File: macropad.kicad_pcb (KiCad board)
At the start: 2 copper layers, 40 x 140 mm, 64 parts, among them J1 SWD, J10 I2C, J11 Keyboard 1, J12 Keyboard 2, J13 Keyboard 2, J2 Keyboard 1, J3 Keyboard 2, J4 Keyboard 1, J5 UART, J6 RS485, J7 Extra, J8 USB_A, J9 CAN, SW1 SW_Push, SW10 Reset, SW2 SW_Push, SW3 SW_Push, SW4 SW_Push, SW5 SW_Push, SW6 SW_Push, U1 AP62250WU, U2 STM32F042K6Tx, U3 MAX490E, U4 MCP2551-I-SN

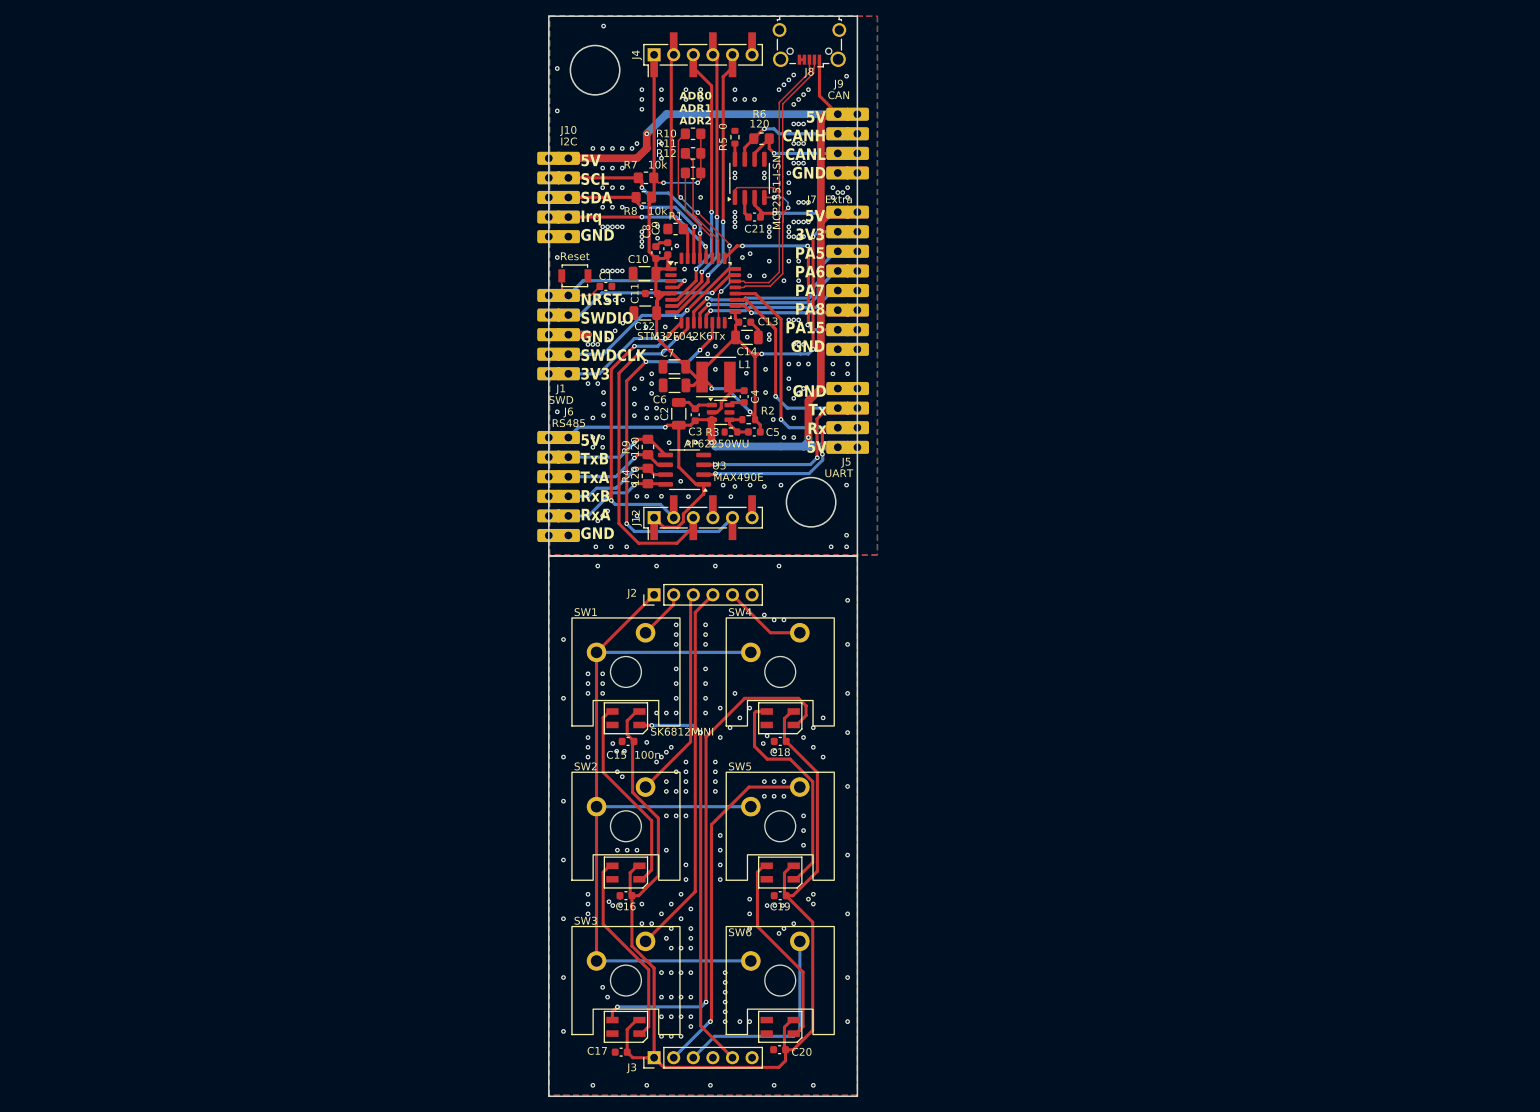
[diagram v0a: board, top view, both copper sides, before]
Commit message: - Created head board tilable up to 4x - Placed and routed lines ToDo: - Print - I2C reanbable
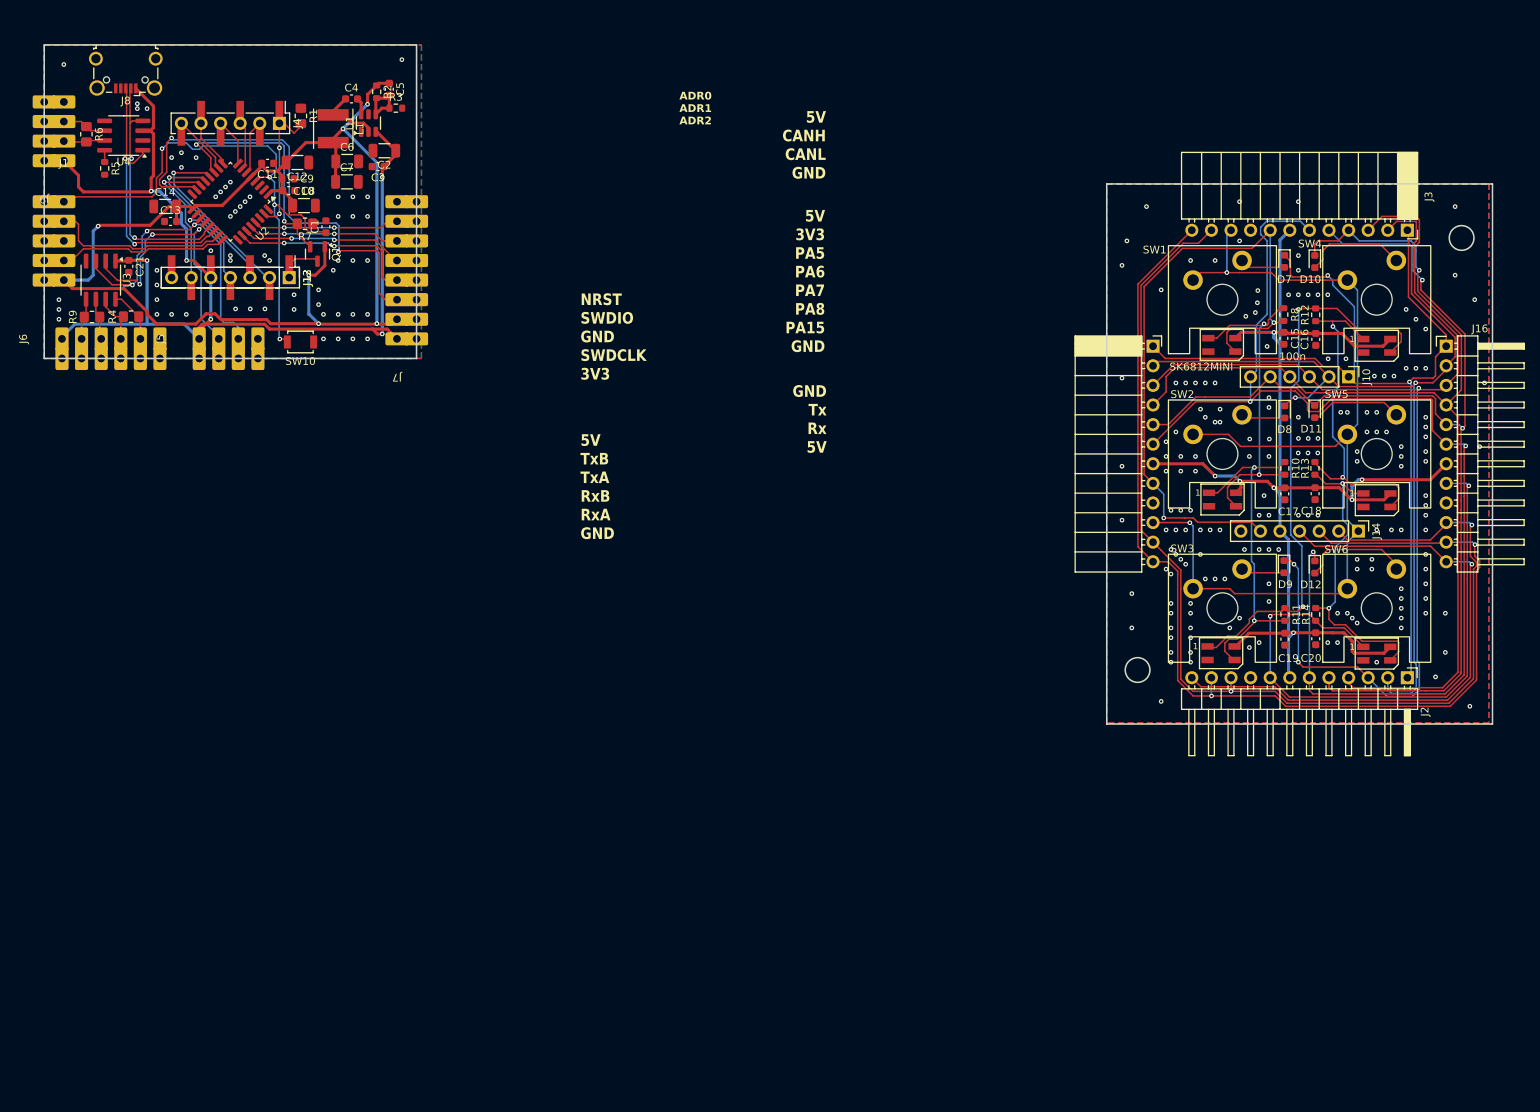
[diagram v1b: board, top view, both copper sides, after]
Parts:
- added D10: D, Diode_SMD:D_0603_1608Metric, F.Cu at (178.6, 73.7)
- added D11: D, Diode_SMD:D_0603_1608Metric, F.Cu at (178.6, 93.2)
- added D12: D, Diode_SMD:D_0603_1608Metric, F.Cu at (178.6, 113.3)
- added D7: D, Diode_SMD:D_0603_1608Metric, F.Cu at (174.6, 73.7)
- added D8: D, Diode_SMD:D_0603_1608Metric, F.Cu at (174.7, 93.2)
- added D9: D, Diode_SMD:D_0603_1608Metric, F.Cu at (174.6, 113.3)
- added J14: Keyboard 2, Connector_PinHeader_2.54mm:PinHeader_1x07_P2.54mm_Vertical, F.Cu at (184.2, 108.7)
- added J15: Conn_01x12_Socket, Connector_PinSocket_2.54mm:PinSocket_1x12_P2.54mm_Horizontal, F.Cu at (157.6, 84.7)
- added J16: Conn_01x12_Pin, Connector_PinHeader_2.54mm:PinHeader_1x12_P2.54mm_Horizontal, F.Cu at (195.6, 84.7)
- added Q1: PNP, Package_TO_SOT_SMD:SOT-23, F.Cu at (49.3, 72.7)
- added R13: R, Resistor_SMD:R_0603_1608Metric, F.Cu at (178.6, 100.5)
- added R14: R, Resistor_SMD:R_0603_1608Metric, F.Cu at (178.7, 119.5)
- J10: value I2C -> Keyboard 1; footprint Library:Conn_Edge_x05 -> Connector_PinHeader_2.54mm:PinHeader_1x06_P2.54mm_Vertical
- J12: footprint Connector_PinHeader_2.54mm:PinHeader_1x06_P2.54mm_Vertical_SMD_Pin1Left -> Connector_PinHeader_2.54mm:PinHeader_1x07_P2.54mm_Vertical_SMD_Pin1Left
- J13: footprint Connector_PinHeader_2.54mm:PinHeader_1x06_P2.54mm_Vertical -> Connector_PinHeader_2.54mm:PinHeader_1x07_P2.54mm_Vertical
- J2: value Keyboard 1 -> Conn_01x12_Pin; footprint Connector_PinHeader_2.54mm:PinHeader_1x06_P2.54mm_Vertical -> Connector_PinHeader_2.54mm:PinHeader_1x12_P2.54mm_Horizontal
- J3: value Keyboard 2 -> Conn_01x12_Socket; footprint Connector_PinHeader_2.54mm:PinHeader_1x06_P2.54mm_Vertical -> Connector_PinSocket_2.54mm:PinSocket_1x12_P2.54mm_Horizontal
- R10, R11, R12, R8: value 10k -> R; footprint Resistor_SMD:R_0805_2012Metric_Pad1.20x1.40mm_HandSolder -> Resistor_SMD:R_0603_1608Metric
- moved J3 145.0 mm to (190.6, 69.7), turned to -90 degrees
- moved C16 114.9 mm to (178.7, 83.8), turned to 90 degrees
- moved C17 112.4 mm to (174.7, 103.8), turned to 90 degrees
- moved J9 105.6 mm to (13.9, 60.6), turned to 180 degrees
- moved J10 105.0 mm to (182.9, 88.7), turned to -90 degrees
- moved C15 99.8 mm to (174.6, 83.7), turned to 90 degrees
- moved J2 98.2 mm to (190.6, 127.7), turned to -90 degrees
- moved R11 97.2 mm to (174.7, 119.5), turned to 90 degrees
- moved D6 91.2 mm to (186.6, 124.5)
- moved D2 91.2 mm to (166.6, 104.6)
- moved D5 91.2 mm to (186.6, 104.6)
- moved D4 91.2 mm to (186.6, 84.6)
- moved D1 91.2 mm to (166.5, 84.5)
- moved SW1 91.1 mm to (166.6, 78.7)
- moved SW2 91.1 mm to (166.6, 98.7)
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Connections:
- C15 pad 1: +5V #2 -> GND #2
- C15 pad 2: GND #2 -> +5V #2
- C16 pad 1: +5V #2 -> GND #2
- C16 pad 2: GND #2 -> +5V #2
- C17 pad 1: +5V #2 -> GND #2
- C17 pad 2: GND #2 -> +5V #2
- C18 pad 1: +5V #2 -> GND #2
- C18 pad 2: GND #2 -> +5V #2
- C19 pad 1: +5V #2 -> GND #2
- C19 pad 2: GND #2 -> +5V #2
- C20 pad 1: +5V #2 -> GND #2
- C20 pad 2: GND #2 -> +5V #2
- D1 pad 3: LED_DATA -> LED_DATA_IN
- D6 pad 1: unconnected-(D6-DOUT-Pad1) -> LED_DATA_OUT
- J10 pad 1: +5V -> H_BTN1
- J10 pad 2: I2C1_SCL -> H_BTN2
- J10 pad 3: I2C1_SDA -> H_BTN3
- J10 pad 4: I2C_Irq -> H_BTN4
- J10 pad 5: VSS -> H_BTN5
- J11 pad 1: VDD -> BOOT0
- J11 pad 2: BOOT0 -> BTN2
- J11 pad 3: BTN2 -> BTN3
- J11 pad 4: BTN3 -> BTN4
- J11 pad 5: BTN4 -> BTN5
- J11 pad 6: VSS -> BTN6
- J12 pad 1: +5V -> GRP1
- J12 pad 2: BTN5 -> GRP2
- J12 pad 3: BTN6 -> GRP3
- J12 pad 4: UNUSED -> GRP4
- J12 pad 5: TIM3_CH3 -> +5V
- J12 pad 6: VSS -> TIM3_CH3
- J13 pad 1: +5V -> GRP1
- J13 pad 2: BTN5 -> GRP2
- J13 pad 3: BTN6 -> GRP3
- J13 pad 4: UNUSED -> GRP4
- J13 pad 5: TIM3_CH3 -> +5V
- J13 pad 6: VSS -> TIM3_CH3
- J2 pad 1: +3.3V #2 -> H_BTN1
- J2 pad 2: Key_1 -> H_BTN2
- J2 pad 3: Key_2 -> H_BTN3
- J2 pad 4: Key_3 -> H_BTN4
- J2 pad 5: Key_4 -> H_BTN5
- J2 pad 6: GND #2 -> H_BTN6
- J3 pad 1: +5V #2 -> H_BTN1
- J3 pad 2: Key_5 -> H_BTN2
- J3 pad 3: Key_6 -> H_BTN3
- J3 pad 4: unconnected-(J3-Pin_4-Pad4) -> H_BTN4
- J3 pad 5: LED_DATA -> H_BTN5
- J3 pad 6: GND #2 -> H_BTN6
- J4 pad 1: VDD -> BOOT0
- J4 pad 2: BOOT0 -> BTN2
- J4 pad 3: BTN2 -> BTN3
- J4 pad 4: BTN3 -> BTN4
- J4 pad 5: BTN4 -> BTN5
- J4 pad 6: VSS -> BTN6
- J7 pad 3: PA5 -> PB1
- J7 pad 4: PA6 -> PB3
- J7 pad 5: PA7 -> PB4
- J7 pad 6: PA8 -> PB5
- J7 pad 7: PA15 -> PB6
- R10 pad 1: I2C_ADR0 -> Net-(D1-DOUT)
- R10 pad 2: VDD -> Net-(D2-DOUT)
- R11 pad 1: I2C_ADR1 -> Net-(D2-DOUT)
- R11 pad 2: VDD -> Net-(D3-DOUT)
- R12 pad 1: I2C_ADR2 -> Net-(D3-DOUT)
- R12 pad 2: VDD -> Net-(D4-DOUT)
- R7 pad 1: I2C1_SCL -> VSS
- R7 pad 2: VDD -> Net-(Q1-B)
- R8 pad 1: I2C1_SDA -> LED_DATA_IN
- R8 pad 2: VDD -> Net-(D1-DOUT)
- SW1 pad 1: +3.3V #2 -> H_GRP1
- SW1 pad 2: Key_1 -> Net-(D7-A)
- SW2 pad 1: +3.3V #2 -> H_GRP1
- SW2 pad 2: Key_2 -> Net-(D8-A)
- SW3 pad 1: +3.3V #2 -> H_GRP1
- SW3 pad 2: Key_3 -> Net-(D9-A)
- SW4 pad 1: +3.3V #2 -> H_GRP1
- SW4 pad 2: Key_4 -> Net-(D10-A)
- SW5 pad 1: +3.3V #2 -> H_GRP1
- SW5 pad 2: Key_5 -> Net-(D11-A)
- SW6 pad 1: +3.3V #2 -> H_GRP1
- SW6 pad 2: Key_6 -> Net-(D12-A)
- U2 pad 11: PA5 -> Net-(Q1-B)
- U2 pad 12: PA6 -> GRP2
- U2 pad 13: PA7 -> GRP3
- U2 pad 15: I2C_ADR0 -> PB1
- U2 pad 18: PA8 -> GRP4
- U2 pad 25: PA15 -> unconnected-(U2-PA15-Pad25)
- U2 pad 26: I2C_ADR1 -> PB3
- U2 pad 27: I2C_ADR2 -> PB4
- U2 pad 28: I2C_Irq -> PB5
- U2 pad 29: I2C1_SCL -> PB6
- U2 pad 30: I2C1_SDA -> unconnected-(U2-PB7-Pad30)
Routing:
- net H_BTN6: track 0.00 -> 152.2 mm, vias 0 -> 3
- net H_GRP3: track 0.00 -> 147.5 mm, vias 0 -> 2
- net H_GRP2: track 0.00 -> 146.8 mm, vias 0 -> 2
- net H_BTN3: track 0.00 -> 144.5 mm, vias 0 -> 3
- net H_BTN5: track 0.00 -> 137.3 mm, vias 0 -> 2
- net H_BTN4: track 0.00 -> 134.6 mm, vias 0 -> 1
- net H_GRP1: track 0.00 -> 125.0 mm, vias 0 -> 2
- net H_BTN1: track 0.00 -> 122.4 mm, vias 0 -> 2
- net H_BTN2: track 0.00 -> 119.9 mm, vias 0 -> 2
- net +3.3V #2: track 110.6 -> 0.00 mm
- net LED_DATA_IN: track 0.00 -> 86.7 mm, vias 0 -> 2
- net H_GRP4: track 0.00 -> 77.4 mm, vias 0 -> 1
- net LED_DATA_OUT: track 0.00 -> 77.4 mm, vias 0 -> 2
- net PB1: track 0.00 -> 60.3 mm, vias 0 -> 2
- net LED_DATA: track 52.2 -> 0.00 mm, vias 2 -> 0
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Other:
- board size 40 x 140 mm -> 187.7 x 88 mm
- board text removed: "5V SCL SDA Irq GND"

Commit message: - Silkscreen positions fixed
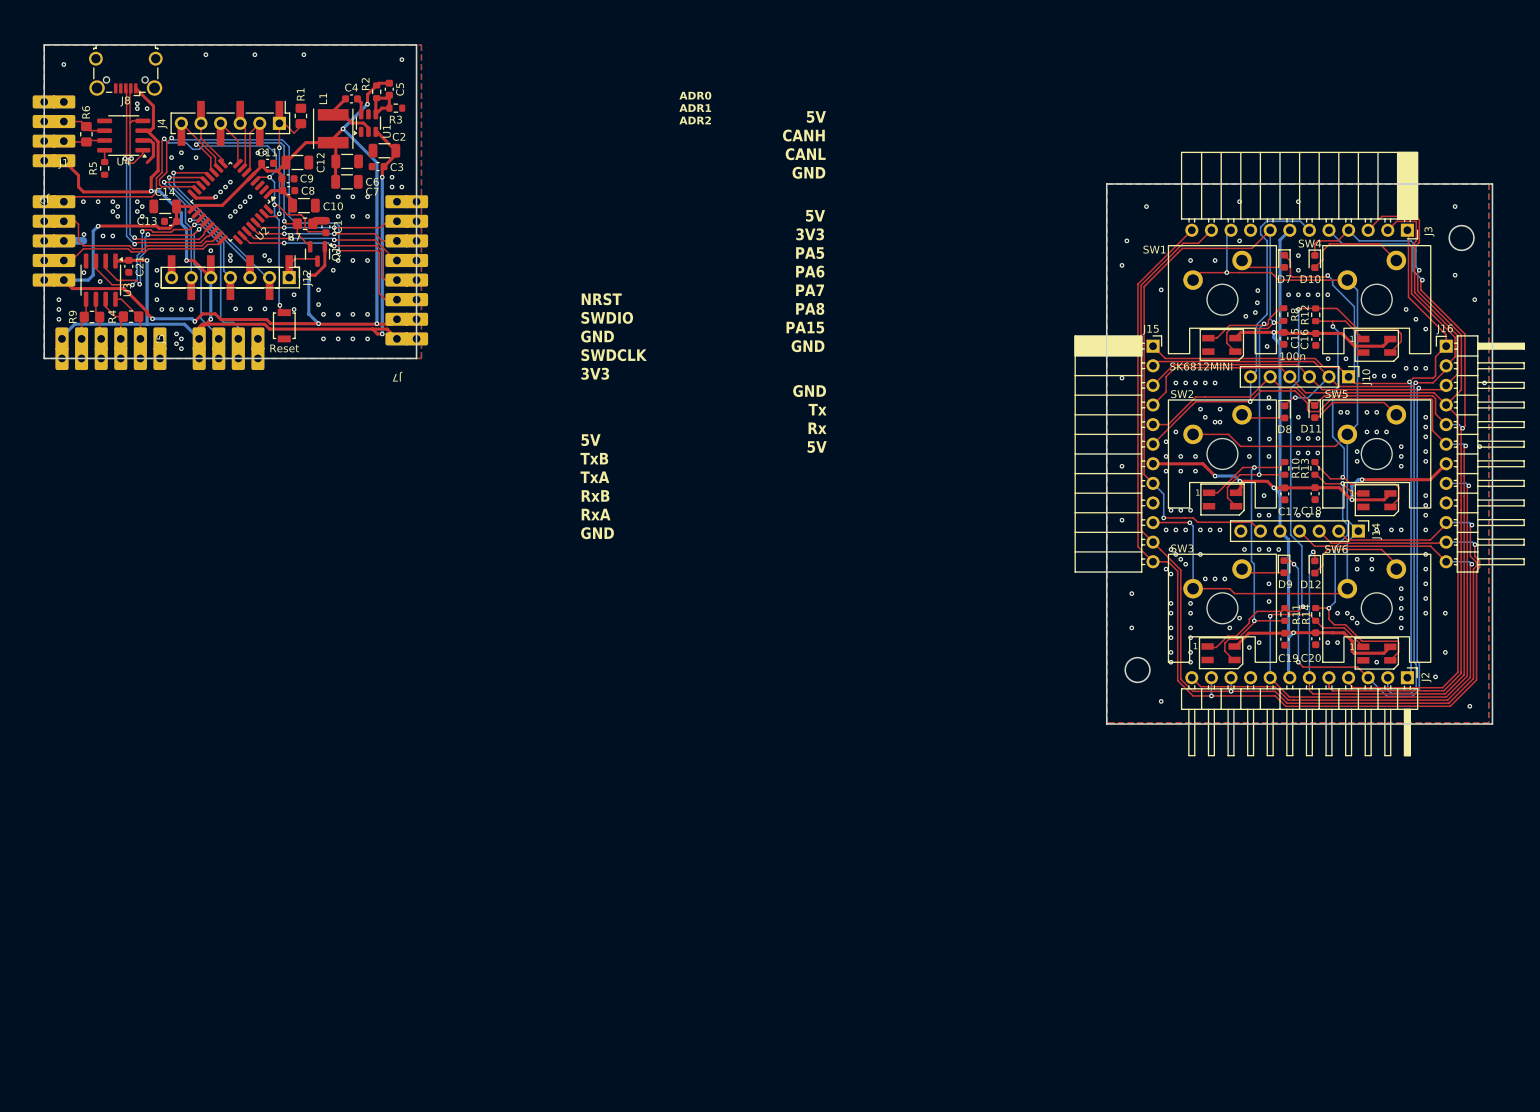
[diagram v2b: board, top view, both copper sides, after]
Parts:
- moved SW10 2.97 mm to (45.0, 82.0), turned to 90 degrees
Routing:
- net VSS: track 0.00 -> 12.7 mm, vias 57 -> 85
- net NRST: track 71.5 -> 68.2 mm
- net +5V: track 143.4 -> 144.6 mm
- net VDD: track 159.8 -> 158.9 mm, vias 6 -> 8
- net USART1_TX: track 40.3 -> 40.9 mm

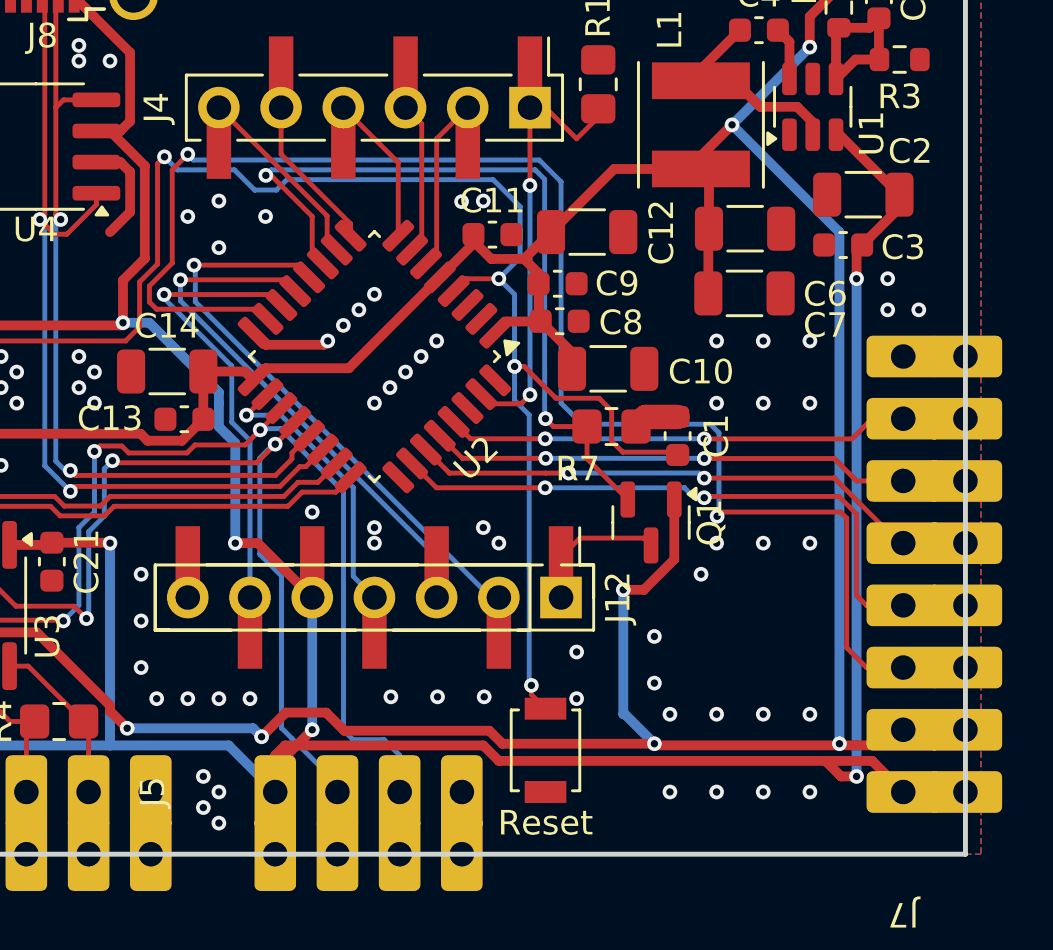
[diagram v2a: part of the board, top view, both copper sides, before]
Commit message: - Added Pull Ups for I2C - Added second reset button on bottom side
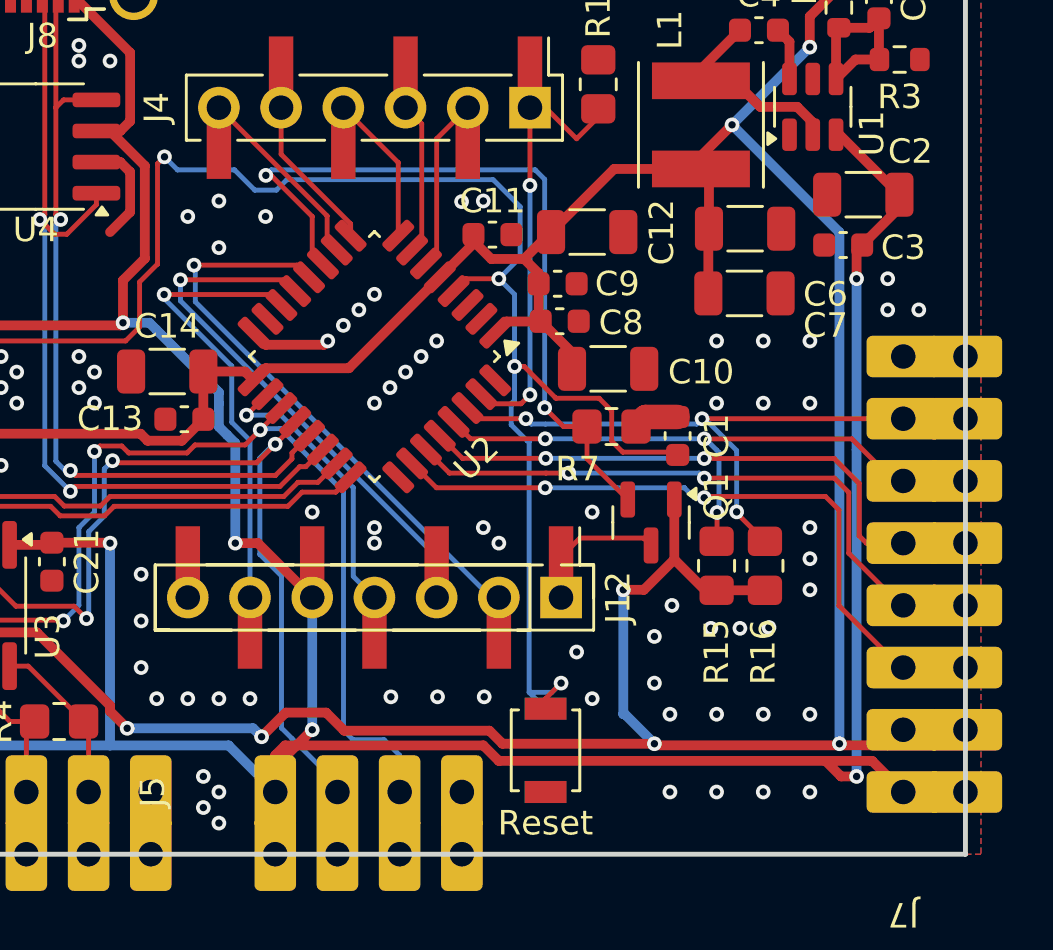
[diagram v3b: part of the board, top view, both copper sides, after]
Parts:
- added R15: 10k, Resistor_SMD:R_0805_2012Metric_Pad1.20x1.40mm_HandSolder, F.Cu at (52.0, 74.5)
- added R16: 10k, Resistor_SMD:R_0805_2012Metric_Pad1.20x1.40mm_HandSolder, F.Cu at (54.0, 74.5)
- added SW11: Reset, Button_Switch_SMD:SW_SPST_B3U-1000P, B.Cu at (45.0, 82.0)
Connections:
- J7 pad 3: PB1 -> PB3
- J7 pad 4: PB3 -> PB4
- J7 pad 5: PB4 -> PB5
- J7 pad 6: PB5 -> PB6
- J7 pad 7: PB6 -> PB7
- U2 pad 15: PB1 -> unconnected-(U2-PB1-Pad15)
- U2 pad 30: unconnected-(U2-PB7-Pad30) -> PB7
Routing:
- net PB1: track 60.3 -> 0.00 mm, vias 2 -> 0
- net PB7: track 0.00 -> 24.3 mm, vias 0 -> 3
- net PB6: track 19.0 -> 23.9 mm, vias 2 -> 3
- net VDD: track 158.9 -> 163.1 mm
- net NRST: track 68.2 -> 71.1 mm
- net PB4: track 21.1 -> 23.6 mm
- net PB5: track 19.7 -> 22.0 mm
- net PB3: track 24.5 -> 25.8 mm
- net VSS: vias 85 -> 89
